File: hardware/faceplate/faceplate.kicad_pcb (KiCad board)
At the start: 2 copper layers, 30 x 128.5 mm, 13 parts

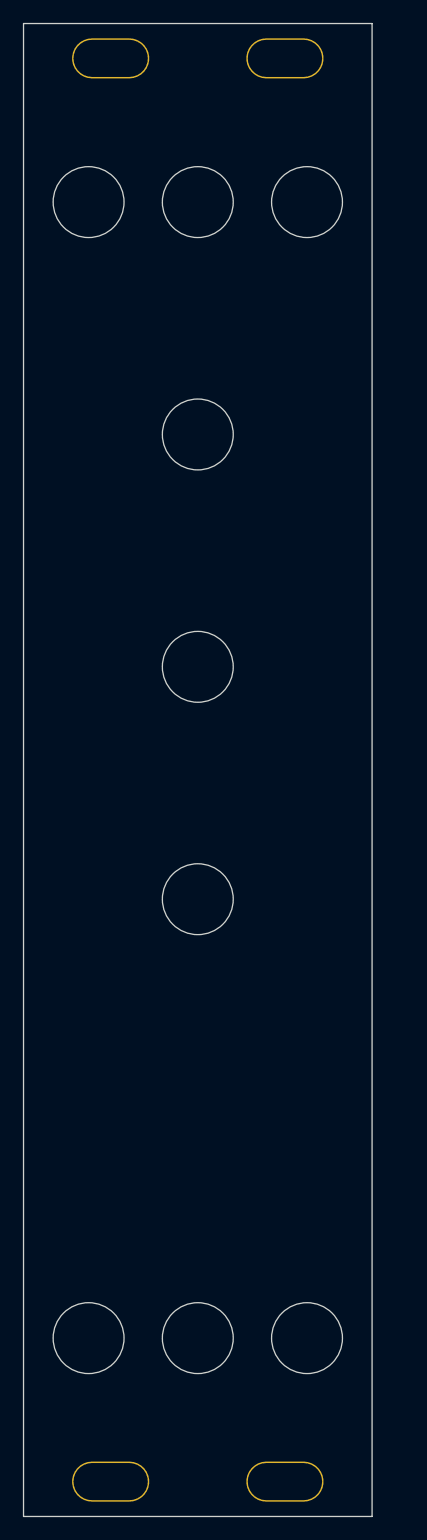
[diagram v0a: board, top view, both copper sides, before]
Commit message: Add adornment to the faceplate
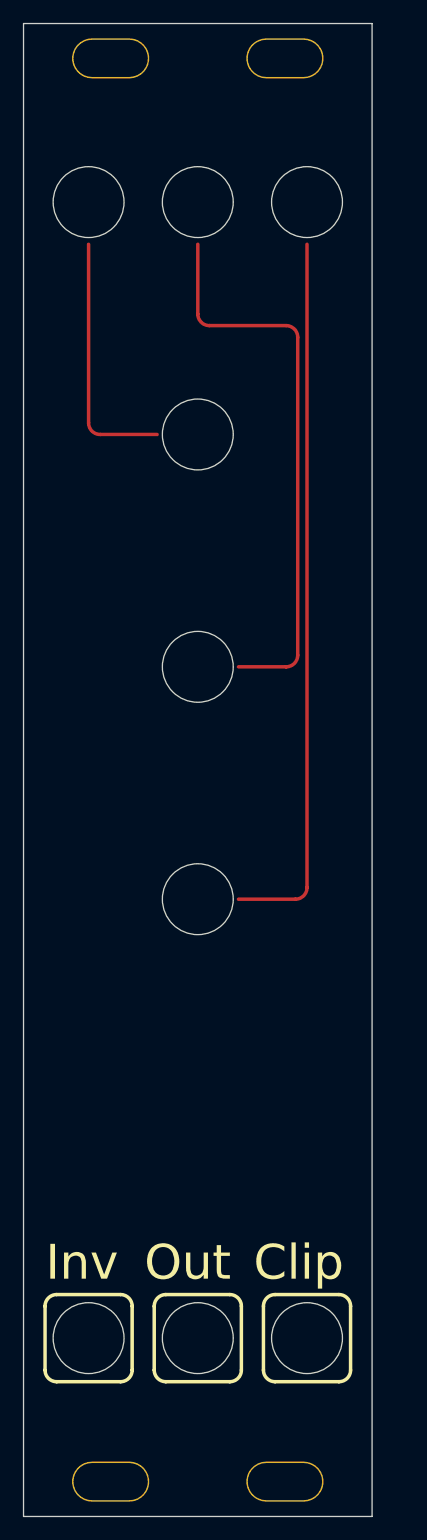
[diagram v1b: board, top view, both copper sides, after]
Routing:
- net (no net): track 0.00 -> 132.3 mm
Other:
- board text added: "Clip"
- board text added: "Inv"
- board text added: "Out"

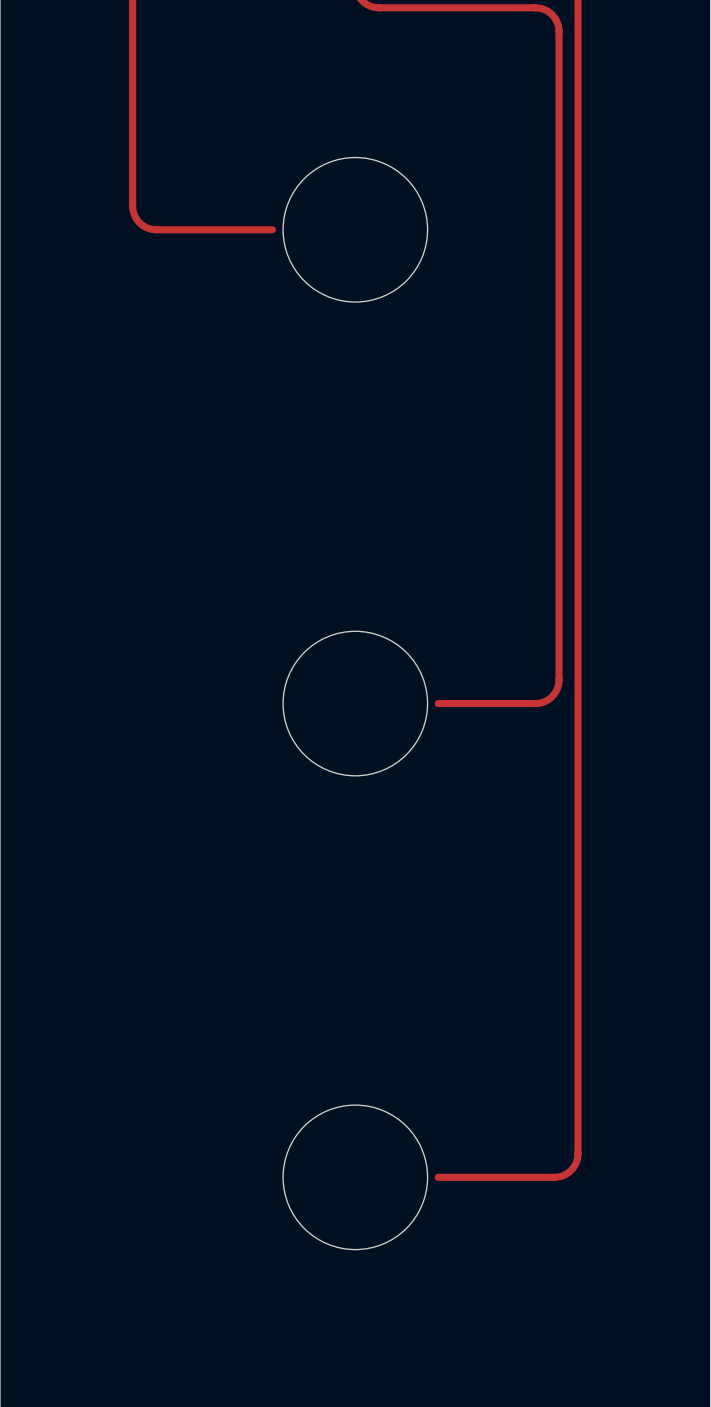
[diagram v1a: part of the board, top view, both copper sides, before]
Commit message: Up size the faceplate drill size for the pots
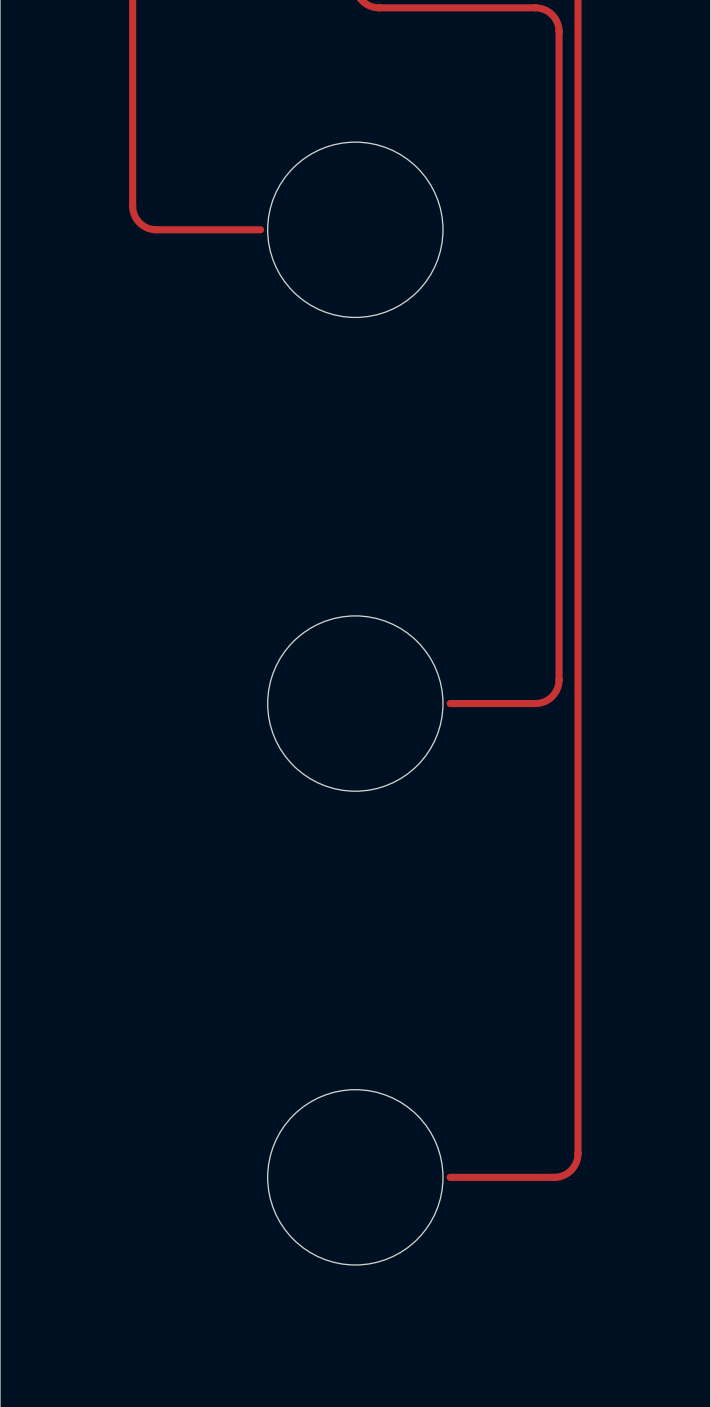
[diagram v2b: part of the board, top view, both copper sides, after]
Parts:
- REF** (x3): value 6mm_Jack -> RK097_Vertical_Potentiometer; footprint ModularMountingHoles:6mm_Jack -> ModularMountingHoles:RK097_Vertical_Potentiometer
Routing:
- net (no net): track 132.3 -> 130.8 mm
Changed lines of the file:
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@@
 	)
 	(net 0 "")
-	(footprint "ModularMountingHoles:6mm_Jack"
+	(footprint "ModularMountingHoles:RK097_Vertical_Potentiometer"
 		(layer "F.Cu")
 		(at 65 125.37)
@@
 			)
 		)
-		(property "Value" "6mm_Jack"
+		(property "Value" "RK097_Vertical_Potentiometer"
 			(at 0 7.35 0)
 			(layer "F.Fab")
@@
 		(pad "" np_thru_hole circle
 			(at 0 0)
-			(size 6.1 6.1)
-			(drill 6.1)
+			(size 7.4 7.4)
+			(drill 7.4)
 			(layers "*.Cu" "*.Mask")
 		)
 		(embedded_fonts no)
 	)
-	(footprint "ModularMountingHoles:6mm_Jack"
+	(footprint "ModularMountingHoles:RK097_Vertical_Potentiometer"
 		(layer "F.Cu")
 		(at 65 85.37)
@@
 			)
 		)
-		(property "Value" "6mm_Jack"
+		(property "Value" "RK097_Vertical_Potentiometer"
 			(at 0 7.35 0)
 			(layer "F.Fab")
@@
 		(pad "" np_thru_hole circle
 			(at 0 0)
-			(size 6.1 6.1)
-			(drill 6.1)
+			(size 7.4 7.4)
+			(drill 7.4)
 			(layers "*.Cu" "*.Mask")
 		)
@@
 		(embedded_fonts no)
 	)
-	(footprint "ModularMountingHoles:6mm_Jack"
+	(footprint "ModularMountingHoles:RK097_Vertical_Potentiometer"
 		(layer "F.Cu")
 		(at 65 105.37)
@@
 			)
 		)
-		(property "Value" "6mm_Jack"
+		(property "Value" "RK097_Vertical_Potentiometer"
 			(at 0 7.35 0)
 			(layer "F.Fab")
@@
 		(pad "" np_thru_hole circle
 			(at 0 0)
-			(size 6.1 6.1)
-			(drill 6.1)
+			(size 7.4 7.4)
+			(drill 7.4)
 			(layers "*.Cu" "*.Mask")
 		)
@@
 	)
 	(gr_line
-		(start 68.5 125.37)
+		(start 69 125.37)
 		(end 73.4 125.37)
 		(stroke
@@
 	(gr_line
 		(start 56.6 85.37)
-		(end 61.5 85.37)
+		(end 61 85.37)
 		(stroke
 			(width 0.3)
@@
 	)
 	(gr_line
-		(start 68.5 105.37)
+		(start 69 105.37)
 		(end 72.6 105.37)
 		(stroke
@@
 	)
 	(segment
-		(start 61.5 85.37)
+		(start 61 85.37)
 		(end 56.6 85.37)
 		(width 0.3)
@@
 	(segment
 		(start 72.6 105.37)
-		(end 68.5 105.37)
+		(end 69 105.37)
 		(width 0.3)
 		(layer "F.Cu")
@@
 	)
 	(segment
-		(start 68.5 125.37)
+		(start 69 125.37)
 		(end 73.4 125.37)
 		(width 0.3)
